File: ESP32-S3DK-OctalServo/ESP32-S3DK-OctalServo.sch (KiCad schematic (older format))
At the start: 9 parts, among them J101 + 5V Servo -, J102 Servo 1, J103 Servo 2, J104 Servo 3, J105 Servo 4, J106 Servo 5, J107 Servo 6, J108 Servo 7, J109 Servo 8

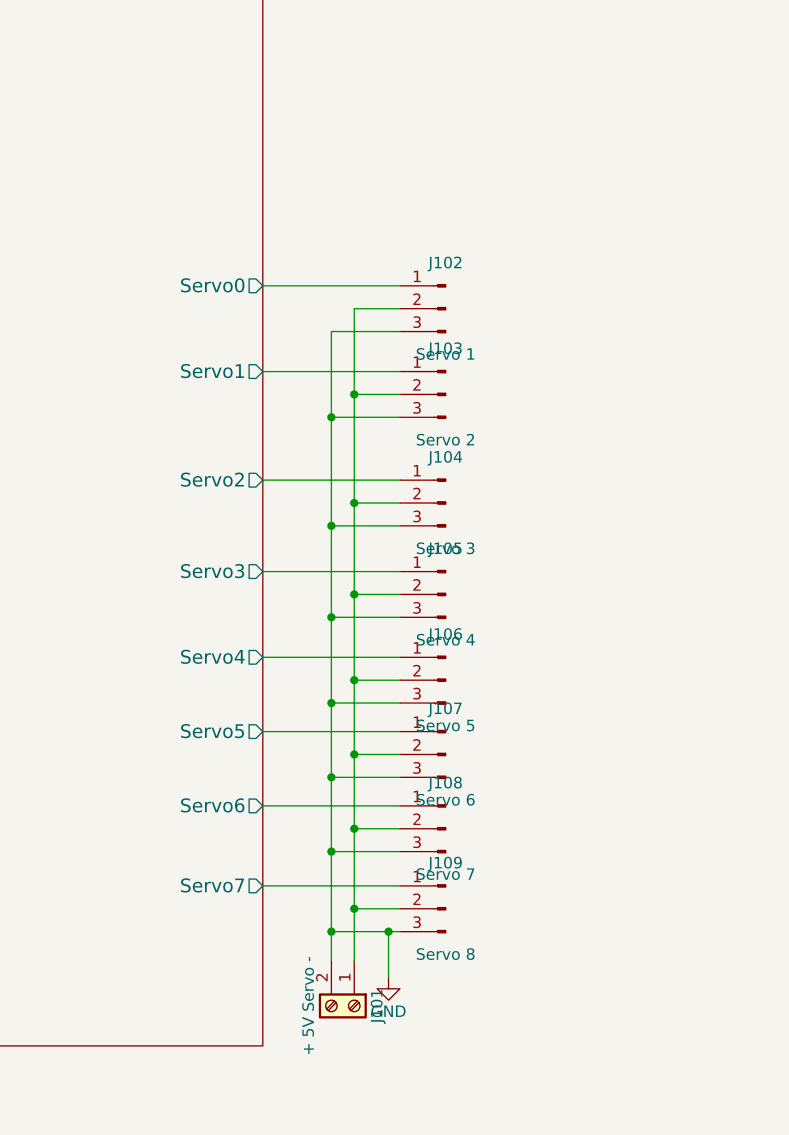
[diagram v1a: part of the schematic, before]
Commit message: Add 3V3=>5V level shifters (74LS125s) to servo control lines.
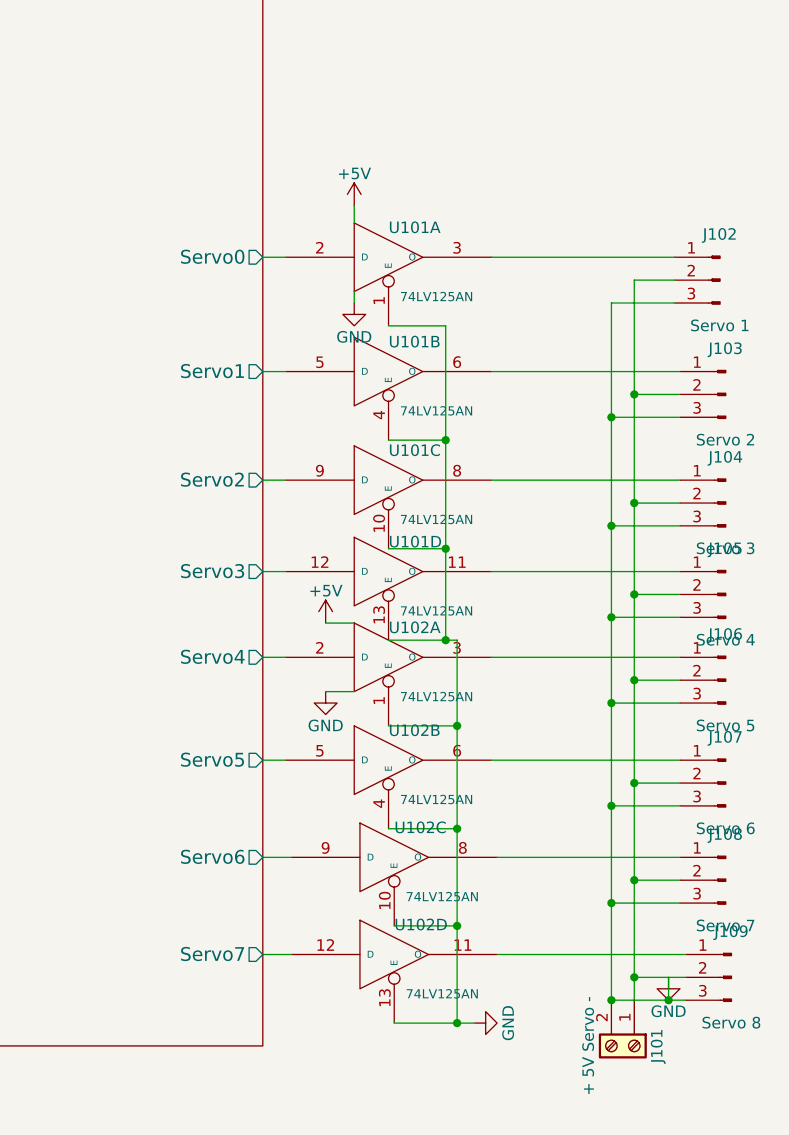
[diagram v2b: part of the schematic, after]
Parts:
- added U101, U102: 74LV125AN, Housings_SOIC:SOIC-14_3.9x8.7mm_Pitch1.27mm, symbol 74LV125AN
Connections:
- net GND: now also U101.1 (E), U101.10 (E), U101.13 (E), U101.4 (E), U101.7 (GND), U101.7 (GND), U101.7 (GND), U101.7 (GND), U102.1 (E), U102.10 (E), U102.13 (E), U102.4 (E), U102.7 (GND), U102.7 (GND), U102.7 (GND), U102.7 (GND)
- net MCU/Servo0: now also U101.2 (D); no longer J102.1 (Pin_1)
- net MCU/Servo1: now also U101.5 (D); no longer J103.1 (Pin_1)
- net MCU/Servo2: now also U101.9 (D); no longer J104.1 (Pin_1)
- net MCU/Servo3: now also U101.12 (D); no longer J105.1 (Pin_1)
- net MCU/Servo4: now also U102.2 (D); no longer J106.1 (Pin_1)
- net MCU/Servo5: now also U102.5 (D); no longer J107.1 (Pin_1)
- net MCU/Servo6: now also U102.9 (D); no longer J108.1 (Pin_1)
- net MCU/Servo7: now also U102.12 (D); no longer J109.1 (Pin_1)
- new net: J109.1 (Pin_1), U102.11 (O)
- new net: J108.1 (Pin_1), U102.8 (O)
- new net: J107.1 (Pin_1), U102.6 (O)
- new net: J106.1 (Pin_1), U102.3 (O)
- new net: J105.1 (Pin_1), U101.11 (O)
- new net: J104.1 (Pin_1), U101.8 (O)
- new net: J103.1 (Pin_1), U101.6 (O)
- new net: J102.1 (Pin_1), U101.3 (O)
- new net +5V: U101.14 (VCC), U101.14 (VCC), U101.14 (VCC), U101.14 (VCC), U102.14 (VCC), U102.14 (VCC), U102.14 (VCC), U102.14 (VCC)
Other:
- moved on the sheet: J101, J102, J103, J104, J105, J106, J107, J108, J109

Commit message: Add 3V3=>5V level shifters (74LS125s) to servo control lines.
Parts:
- U101, U102: Mouser Part Number 595-SN74LS125ANSR -> 771-AHCT125D118
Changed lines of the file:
@@
 F 2 "Housings_SOIC:SOIC-14_3.9x8.7mm_Pitch1.27mm" H 7275 3000 60  0001 C CNN
 F 3 "" H 7275 3000 60  0000 C CNN
-F 4 "595-SN74LS125ANSR" H 7275 3000 60  0001 C CNN "Mouser Part Number"
+F 4 "771-AHCT125D118" H 7275 3000 60  0001 C CNN "Mouser Part Number"
 	1    7275 3000
 	1    0    0    -1
@@
 F 2 "Housings_SOIC:SOIC-14_3.9x8.7mm_Pitch1.27mm" H 7275 4750 60  0001 C CNN
 F 3 "" H 7275 4750 60  0000 C CNN
-F 4 "595-SN74LS125ANSR" H 7275 4750 60  0001 C CNN "Mouser Part Number"
+F 4 "771-AHCT125D118" H 7275 4750 60  0001 C CNN "Mouser Part Number"
 	1    7275 4750
 	1    0    0    -1

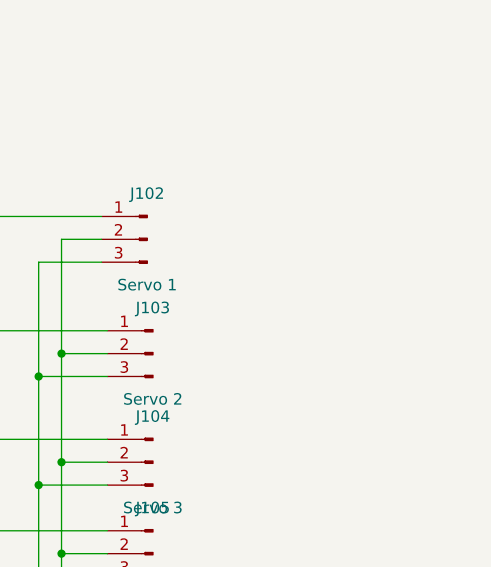
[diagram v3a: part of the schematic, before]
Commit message: Add bypass caps.
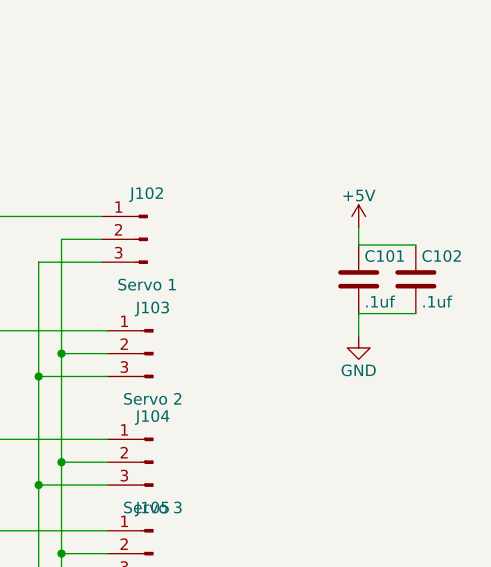
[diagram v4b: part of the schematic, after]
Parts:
- added C101, C102: .1uf, Capacitors_SMD:C_0603, symbol C
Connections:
- net +5V: now also C101.1, C102.1
- net GND: now also C101.2, C102.2
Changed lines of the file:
@@
 $EndComp
 Connection ~ 7575 6350
+$Comp
+L C C101
+U 1 1 63DBFB5B
+P 9650 3275
+F 0 "C101" H 9675 3375 50  0000 L CNN
+F 1 ".1uf" H 9675 3175 50  0000 L CNN
+F 2 "Capacitors_SMD:C_0603" H 9688 3125 50  0001 C CNN
+F 3 "" H 9650 3275 50  0001 C CNN
+	1    9650 3275
+	1    0    0    -1
+$EndComp
+$Comp
+L C C102
+U 1 1 63DBFC76
+P 9900 3275
+F 0 "C102" H 9925 3375 50  0000 L CNN
+F 1 ".1uf" H 9925 3175 50  0000 L CNN
+F 2 "Capacitors_SMD:C_0603" H 9938 3125 50  0001 C CNN
+F 3 "" H 9900 3275 50  0001 C CNN
+	1    9900 3275
+	1    0    0    -1
+$EndComp
+$Comp
+L +5V #PWR07
+U 1 1 63DBFDE4
+P 9650 3050
+F 0 "#PWR07" H 9650 2900 50  0001 C CNN
+F 1 "+5V" H 9650 3190 50  0000 C CNN
+F 2 "" H 9650 3050 50  0001 C CNN
+F 3 "" H 9650 3050 50  0001 C CNN
+	1    9650 3050
+	1    0    0    -1
+$EndComp
+$Comp
+L GND #PWR08
+U 1 1 63DBFE66
+P 9650 3525
+F 0 "#PWR08" H 9650 3275 50  0001 C CNN
+F 1 "GND" H 9650 3375 50  0000 C CNN
+F 2 "" H 9650 3525 50  0001 C CNN
+F 3 "" H 9650 3525 50  0001 C CNN
+	1    9650 3525
+	1    0    0    -1
+$EndComp
+Wire Wire Line
+	9650 3050 9650 3125
+Wire Wire Line
+	9650 3125 9900 3125
+Wire Wire Line
+	9900 3425 9650 3425
+Wire Wire Line
+	9650 3425 9650 3525
 $EndSCHEMATC

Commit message: Rescue schematics
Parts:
- U101, U102: symbol 74LV125AN -> 74LV125AN-RESCUE-ESP32-S3DK-OctalServo
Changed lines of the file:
@@
 EESchema Schematic File Version 2
+LIBS:ESP32-S3DK-OctalServo-rescue
 LIBS:power
 LIBS:device
@@
 $EndComp
 $Comp
-L 74LV125AN U101
+L 74LV125AN-RESCUE-ESP32-S3DK-OctalServo U101
 U 1 1 63DAB544
 P 7275 3000
@@
 $EndComp
 $Comp
-L 74LV125AN U101
+L 74LV125AN-RESCUE-ESP32-S3DK-OctalServo U101
 U 3 1 63DAD0D7
 P 7275 3975
@@
 $EndComp
 $Comp
-L 74LV125AN U101
+L 74LV125AN-RESCUE-ESP32-S3DK-OctalServo U101
 U 2 1 63DAD170
 P 7275 3500
@@
 $EndComp
 $Comp
-L 74LV125AN U101
+L 74LV125AN-RESCUE-ESP32-S3DK-OctalServo U101
 U 4 1 63DAD484
 P 7275 4375
@@
 $EndComp
 $Comp
-L 74LV125AN U102
+L 74LV125AN-RESCUE-ESP32-S3DK-OctalServo U102
 U 1 1 63DB53B3
 P 7275 4750
@@
 $EndComp
 $Comp
-L 74LV125AN U102
+L 74LV125AN-RESCUE-ESP32-S3DK-OctalServo U102
 U 3 1 63DB53BA
 P 7300 5625
@@
 $EndComp
 $Comp
-L 74LV125AN U102
+L 74LV125AN-RESCUE-ESP32-S3DK-OctalServo U102
 U 2 1 63DB53C1
 P 7275 5200
@@
 $EndComp
 $Comp
-L 74LV125AN U102
+L 74LV125AN-RESCUE-ESP32-S3DK-OctalServo U102
 U 4 1 63DB53C8
 P 7300 6050
